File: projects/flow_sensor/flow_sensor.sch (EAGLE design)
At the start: 98 parts, among them IC1 TPS61201, IC5 REG1118

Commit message: Added Spi-Bi-Wire to uC, added SPI connections between uC/NFC
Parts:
- removed J1, J2: (no value), SparkFun-Connectors:CONN_02
- added J3: (no value), SparkFun-Connectors:CONN_07
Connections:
- removed net DATA_CLK: U$2.DATA_CLK
- removed net MISO: U$2.I/O_6
- removed net MOSI: U$2.I/O_7
- removed net N$55: J1.2, U$9.~RESET(SBWTDIO)
- removed net N$56: J1.1, U$9.SBWTCK
- new net 3.3V: J3.3
- new net 5V: J3.2
- new net CLK: U$2.DATA_CLK, U$9.(UCA0CLK/A5)P1.5
- new net RXD: J3.4
- new net SBWTCK: J3.7, U$9.SBWTCK
- new net SBWTDIO: J3.6, U$9.~RESET(SBWTDIO)
- new net SIMO: U$2.I/O_7, U$9.(UCA0TXD/UCA0SIMO)P2.0
- new net SOMI: U$2.I/O_6, U$9.(UCA0RXD/UCA0SOMI)P2.1
- new net STE: U$9.(UCA0STE/A4)P1.4
- new net TXD: J3.5
- net GND: now also J3.1; no longer J2.2
- net VCC: no longer J2.1
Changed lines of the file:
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@@
 <?xml version="1.0" encoding="utf-8"?>
 <!DOCTYPE eagle SYSTEM "eagle.dtd">
-<eagle version="8.5.1">
+<eagle version="8.4.3">
 <drawing>
 <settings>
@@
 <part name="C27" library="SparkFun-Capacitors" deviceset="1.0UF" device="-0603-16V-10%" value="1.0uF"/>
 <part name="C40" library="SparkFun-Capacitors" deviceset="0.1UF" device="-0603-25V-(+80/-20%)" value="0.1uF"/>
-<part name="J1" library="SparkFun-Connectors" deviceset="CONN_02" device=""/>
-<part name="J2" library="SparkFun-Connectors" deviceset="CONN_02" device=""/>
-<part name="GND45" library="SparkFun-PowerSymbols" deviceset="GND2" device=""/>
+<part name="J3" library="SparkFun-Connectors" deviceset="CONN_07" device=""/>
+<part name="GND46" library="SparkFun-PowerSymbols" deviceset="GND2" device=""/>
 </parts>
 <sheets>
@@
 <instance part="C38" gate="G$1" x="96.52" y="2.54"/>
 <instance part="C39" gate="G$1" x="104.14" y="2.54"/>
+<instance part="J3" gate="G$1" x="-63.5" y="20.32" rot="R270"/>
+<instance part="GND46" gate="G$1" x="-68.58" y="2.54"/>
 </instances>
 <busses>
@@
 <wire x1="436.88" y1="-7.62" x2="441.96" y2="-7.62" width="0.1524" layer="91"/>
 <wire x1="441.96" y1="-7.62" x2="441.96" y2="-10.16" width="0.1524" layer="91"/>
+</segment>
+<segment>
+<pinref part="J3" gate="G$1" pin="1"/>
+<wire x1="-68.58" y1="15.24" x2="-68.58" y2="5.08" width="0.1524" layer="91"/>
+<pinref part="GND46" gate="G$1" pin="3.3V"/>
 </segment>
 </net>
@@
 <label x="444.5" y="-35.56" size="1.778" layer="95" rot="MR270"/>
 <pinref part="U$8" gate="G$1" pin="OUT1"/>
+</segment>
+</net>
+<net name="5V" class="0">
+<segment>
+<pinref part="J3" gate="G$1" pin="2"/>
+<wire x1="-66.04" y1="15.24" x2="-66.04" y2="7.62" width="0.1524" layer="91"/>
+<label x="-66.04" y="7.62" size="1.778" layer="95" rot="R270"/>
+</segment>
+</net>
+<net name="3.3V" class="0">
+<segment>
+<pinref part="J3" gate="G$1" pin="3"/>
+<wire x1="-63.5" y1="15.24" x2="-63.5" y2="7.62" width="0.1524" layer="91"/>
+<label x="-63.5" y="7.62" size="1.778" layer="95" rot="R270"/>
+</segment>
+</net>
+<net name="RXD" class="0">
+<segment>
+<pinref part="J3" gate="G$1" pin="4"/>
+<wire x1="-60.96" y1="15.24" x2="-60.96" y2="7.62" width="0.1524" layer="91"/>
+<label x="-60.96" y="7.62" size="1.778" layer="95" rot="R270"/>
+</segment>
+</net>
+<net name="TXD" class="0">
+<segment>
+<pinref part="J3" gate="G$1" pin="5"/>
+<wire x1="-58.42" y1="15.24" x2="-58.42" y2="7.62" width="0.1524" layer="91"/>
+<label x="-58.42" y="7.62" size="1.778" layer="95" rot="R270"/>
+</segment>
+</net>
+<net name="SBWTDIO" class="0">
+<segment>
+<pinref part="J3" gate="G$1" pin="6"/>
+<wire x1="-55.88" y1="15.24" x2="-55.88" y2="7.62" width="0.1524" layer="91"/>
+<label x="-55.88" y="7.62" size="1.778" layer="95" rot="R270"/>
+</segment>
+</net>
+<net name="SBWTCK" class="0">
+<segment>
+<pinref part="J3" gate="G$1" pin="7"/>
+<wire x1="-53.34" y1="15.24" x2="-53.34" y2="7.62" width="0.1524" layer="91"/>
+<label x="-53.34" y="7.62" size="1.778" layer="95" rot="R270"/>
 </segment>
 </net>
@@
 <instance part="C27" gate="G$1" x="218.44" y="43.18" rot="R90"/>
 <instance part="C40" gate="G$1" x="218.44" y="53.34" rot="R90"/>
-<instance part="J1" gate="G$1" x="238.76" y="15.24"/>
-<instance part="J2" gate="G$1" x="233.68" y="17.78" rot="R180"/>
-<instance part="GND45" gate="G$1" x="210.82" y="15.24" rot="R270"/>
 </instances>
 <busses>
@@
 <wire x1="-116.84" y1="45.72" x2="-116.84" y2="53.34" width="0.1524" layer="91"/>
 <label x="-116.84" y="53.34" size="1.6764" layer="95" rot="R90"/>
-</segment>
-</net>
-<net name="DATA_CLK" class="0">
-<segment>
-<pinref part="U$2" gate="G$1" pin="DATA_CLK"/>
-<wire x1="-86.36" y1="43.18" x2="-121.92" y2="43.18" width="0.1524" layer="91"/>
-<wire x1="-121.92" y1="43.18" x2="-121.92" y2="53.34" width="0.1524" layer="91"/>
-<label x="-121.92" y="53.34" size="1.6764" layer="95" rot="R90"/>
-</segment>
-</net>
-<net name="MOSI" class="0">
-<segment>
-<pinref part="U$2" gate="G$1" pin="I/O_7"/>
-<wire x1="-86.36" y1="40.64" x2="-127" y2="40.64" width="0.1524" layer="91"/>
-<wire x1="-127" y1="40.64" x2="-127" y2="53.34" width="0.1524" layer="91"/>
-<label x="-127" y="53.34" size="1.6764" layer="95" rot="R90"/>
-</segment>
-</net>
-<net name="MISO" class="0">
-<segment>
-<pinref part="U$2" gate="G$1" pin="I/O_6"/>
-<wire x1="-86.36" y1="38.1" x2="-132.08" y2="38.1" width="0.1524" layer="91"/>
-<wire x1="-132.08" y1="38.1" x2="-132.08" y2="53.34" width="0.1524" layer="91"/>
-<label x="-132.08" y="53.34" size="1.6764" layer="95" rot="R90"/>
 </segment>
 </net>
@@
 <wire x1="210.82" y1="25.4" x2="256.54" y2="25.4" width="0.1524" layer="91"/>
 </segment>
-<segment>
-<pinref part="J2" gate="G$1" pin="2"/>
-<pinref part="GND45" gate="G$1" pin="3.3V"/>
-<wire x1="226.06" y1="15.24" x2="213.36" y2="15.24" width="0.1524" layer="91"/>
-</segment>
 </net>
 <net name="N$5" class="0">
@@
 <junction x="223.52" y="43.18"/>
 </segment>
-<segment>
-<pinref part="J2" gate="G$1" pin="1"/>
-<wire x1="226.06" y1="17.78" x2="213.36" y2="17.78" width="0.1524" layer="91"/>
-<label x="213.36" y="17.78" size="1.778" layer="95"/>
-</segment>
 </net>
 <net name="N$8" class="0">
@@
 </segment>
 </net>
-<net name="N$55" class="0">
+<net name="SBWTDIO" class="0">
 <segment>
 <pinref part="U$9" gate="G$1" pin="~RESET(SBWTDIO)"/>
-<pinref part="J1" gate="G$1" pin="2"/>
-<wire x1="256.54" y1="17.78" x2="246.38" y2="17.78" width="0.1524" layer="91"/>
-</segment>
-</net>
-<net name="N$56" class="0">
+<wire x1="256.54" y1="17.78" x2="233.68" y2="17.78" width="0.1524" layer="91"/>
+<label x="233.68" y="17.78" size="1.778" layer="95" rot="R180"/>
+</segment>
+</net>
+<net name="SBWTCK" class="0">
 <segment>
 <pinref part="U$9" gate="G$1" pin="SBWTCK"/>
-<pinref part="J1" gate="G$1" pin="1"/>
-<wire x1="256.54" y1="15.24" x2="246.38" y2="15.24" width="0.1524" layer="91"/>
-</segment>
-</net>
+<wire x1="256.54" y1="15.24" x2="233.68" y2="15.24" width="0.1524" layer="91"/>
+<label x="233.68" y="15.24" size="1.778" layer="95" rot="R180"/>
+</segment>
+</net>
+<net name="SIMO" class="0">
+<segment>
+<pinref part="U$9" gate="G$1" pin="(UCA0TXD/UCA0SIMO)P2.0"/>
+<wire x1="317.5" y1="15.24" x2="325.12" y2="15.24" width="0.1524" layer="91"/>
+<label x="325.12" y="15.24" size="1.778" layer="95"/>
+</segment>
+<segment>
+<pinref part="U$2" gate="G$1" pin="I/O_7"/>
+<wire x1="-86.36" y1="40.64" x2="-127" y2="40.64" width="0.1524" layer="91"/>
+<wire x1="-127" y1="40.64" x2="-127" y2="53.34" width="0.1524" layer="91"/>
+<label x="-127" y="53.34" size="1.6764" layer="95" rot="R90"/>
+</segment>
+</net>
+<net name="SOMI" class="0">
+<segment>
+<pinref part="U$9" gate="G$1" pin="(UCA0RXD/UCA0SOMI)P2.1"/>
+<wire x1="317.5" y1="12.7" x2="325.12" y2="12.7" width="0.1524" layer="91"/>
+<label x="325.12" y="12.7" size="1.778" layer="95"/>
+</segment>
+<segment>
+<pinref part="U$2" gate="G$1" pin="I/O_6"/>
+<wire x1="-86.36" y1="38.1" x2="-132.08" y2="38.1" width="0.1524" layer="91"/>
+<wire x1="-132.08" y1="38.1" x2="-132.08" y2="53.34" width="0.1524" layer="91"/>
+<label x="-132.08" y="53.34" size="1.6764" layer="95" rot="R90"/>
+</segment>
+</net>
+<net name="STE" class="0">
+<segment>
+<pinref part="U$9" gate="G$1" pin="(UCA0STE/A4)P1.4"/>
+<wire x1="317.5" y1="30.48" x2="325.12" y2="30.48" width="0.1524" layer="91"/>
+<label x="325.12" y="30.48" size="1.778" layer="95"/>
+</segment>
+</net>
+<net name="CLK" class="0">
+<segment>
+<pinref part="U$9" gate="G$1" pin="(UCA0CLK/A5)P1.5"/>
+<wire x1="317.5" y1="27.94" x2="325.12" y2="27.94" width="0.1524" layer="91"/>
+<label x="325.12" y="27.94" size="1.778" layer="95"/>
+</segment>
+<segment>
+<pinref part="U$2" gate="G$1" pin="DATA_CLK"/>
+<wire x1="-86.36" y1="43.18" x2="-121.92" y2="43.18" width="0.1524" layer="91"/>
+<wire x1="-121.92" y1="43.18" x2="-121.92" y2="53.34" width="0.1524" layer="91"/>
+<label x="-121.92" y="53.34" size="1.6764" layer="95" rot="R90"/>
+</segment>
+</net>

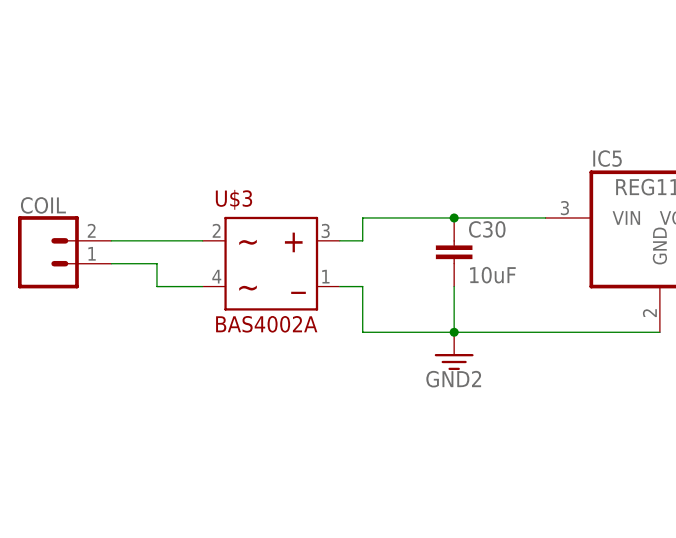
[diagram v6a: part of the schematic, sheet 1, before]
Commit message: Fixed BAS4002A part again
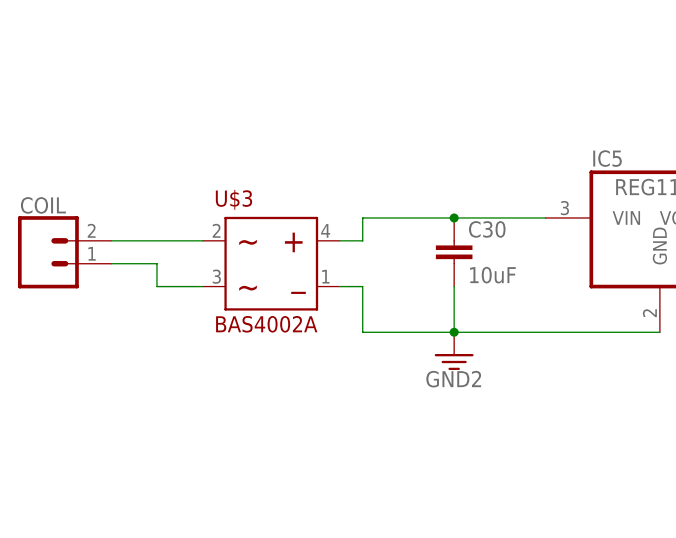
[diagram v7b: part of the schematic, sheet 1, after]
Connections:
- net N$1 renamed POWERCOIL
- net N$27 renamed POWERCOIL'
- net N$30 renamed UNREG+
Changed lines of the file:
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@@
 <?xml version="1.0" encoding="utf-8"?>
 <!DOCTYPE eagle SYSTEM "eagle.dtd">
-<eagle version="8.4.3">
+<eagle version="8.5.1">
 <drawing>
 <settings>
@@
 </segment>
 </net>
-<net name="N$1" class="0">
+<net name="POWERCOIL" class="0">
 <segment>
 <pinref part="COIL" gate="G$1" pin="2"/>
@@
 </segment>
 </net>
-<net name="N$30" class="0">
+<net name="UNREG+" class="0">
 <segment>
 <pinref part="U$3" gate="G$1" pin="+"/>
@@
 </segment>
 </net>
-<net name="N$27" class="0">
+<net name="POWERCOIL'" class="0">
 <segment>
 <pinref part="U$3" gate="G$1" pin="~'"/>

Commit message: Modified sensor: Added mux, reduced op-amps
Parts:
- removed C29, C31, C32, C33, C34, C35, C36: 3uF, SparkFun-Capacitors:4.7UF0603
- removed R16, R17, R18, R19, R20, R21: 10k, SparkFun-Resistors:10KOHM-0603-1/10W-1%
- removed R37: 1.5k, SparkFun-Resistors:8.2KOHM-0603-1/10W-5%
- removed R38: 1.5k, SparkFun-Resistors:1.5KOHM-0603-1/10W-1%
- removed R39: 8.2k, SparkFun-Resistors:1.5KOHM-0603-1/10W-1%
- removed U$5: LM2902, my_library:LM2902
- added C41: 3uF, SparkFun-Capacitors:4.7UF0603
- R11, R29: value 600 -> 8.2k; device SparkFun-Resistors:680OHM-0603-1/10W-5% -> SparkFun-Resistors:8.2KOHM-0603-1/10W-5%
- R22: value 800 -> 1.5k; device SparkFun-Resistors:787OHM-0603-1/10W-1% -> SparkFun-Resistors:8.2KOHM-0603-1/10W-5%
- R23: value 600 -> 1.5k; device SparkFun-Resistors:680OHM-0603-1/10W-5% -> SparkFun-Resistors:1.5KOHM-0603-1/10W-1%
- R24, R31: device SparkFun-Resistors:8.2KOHM-0603-1/10W-5% -> SparkFun-Resistors:1.5KOHM-0603-1/10W-1%
- R25, R32: value 1.5k -> 8.2k
- R26: device SparkFun-Resistors:1.5KOHM-0603-1/10W-1% -> SparkFun-Resistors:8.2KOHM-0603-1/10W-5%
- R27, R30: value 8.2k -> 1.5k
- R28: value 800 -> 8.2k; device SparkFun-Resistors:787OHM-0603-1/10W-1% -> SparkFun-Resistors:1.5KOHM-0603-1/10W-1%
- R33: value 8.2k -> 800; device SparkFun-Resistors:1.5KOHM-0603-1/10W-1% -> SparkFun-Resistors:787OHM-0603-1/10W-1%
- R35: value 600 -> 800; device SparkFun-Resistors:680OHM-0603-1/10W-5% -> SparkFun-Resistors:787OHM-0603-1/10W-1%
- R36: value 8.2k -> 600; device SparkFun-Resistors:8.2KOHM-0603-1/10W-5% -> SparkFun-Resistors:787OHM-0603-1/10W-1%
- U$7: value AD8222 -> MAX4634; device my_library:AD8222 -> my_library:MAX4634
- U$8: value AD8222 -> AD8295; device my_library:AD8222 -> my_library:AD8295
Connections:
- removed net N$31: C34.1, R16.2, R17.1
- removed net N$36: C31.1, R17.2
- removed net N$38: C35.1, R18.2, R19.1
- removed net N$39: C32.1, R19.2
- removed net N$41: C36.1, R20.2, R21.1
- removed net N$42: C33.1, R21.2
- removed net N$47: R22.1, U$6.RG2
- removed net N$49: R23.1, U$6.RG1
- removed net N$52: R34.2, U$8.RG2'
- removed net N$53: R35.1, U$8.RG1
- removed net N$54: R35.2, U$8.RG1'
- removed net OPAMP1_OUT: C29.2, U$4.+IN1, U$5.IN1-, U$5.OUT1
- removed net OPAMP2_OUT: C34.2, U$5.IN2-, U$5.OUT2, U$6.+IN1
- removed net OPAMP3_IN: R18.1, U$7.OUT2
- removed net OPAMP3_OUT: C35.2, U$5.IN3-, U$5.OUT3, U$7.+IN1
- removed net OPAMP4_IN: R20.1, U$8.OUT2
- removed net OPAMP4_OUT: C36.2, U$5.IN4-, U$5.OUT4, U$8.+IN1
- removed net SENSOR_ADC1: U$4.OUT1
- removed net SENSOR_ADC2: U$6.OUT1
- removed net SENSOR_ADC3: U$7.OUT1
- removed net SENSOR_ADC4: U$8.OUT1
- new net MUX_A0: U$7.A0
- new net MUX_A1: U$7.A1
- new net MUX_EN: U$7.EN
- new net N$1: R11.2, R23.1, U$4.-IN2
- new net N$27: R30.1, R32.2, U$6.+IN2
- new net N$30: R33.1, U$6.RG2
- new net SENSOR_OUT: U$8.OUT
- net 3.3V: now also U$7.GND, U$8.-IN
- net GND: now also R22.2, R23.2, R27.2, R30.2; no longer C31.2, C32.2, C33.2, R25.2, R32.2, R37.2, R38.2, U$4.-IN1, U$5.VCC-, U$6.-IN1, U$7.-IN1, U$7.-VS, U$7.REF1, U$7.REF2, U$8.-IN1, U$8.-VS, U$8.REF1, U$8.REF2
- net N$18: now also U$7.COM; no longer U$4.OUT2
- net N$19: now also U$8.A2+IN; no longer U$5.IN1+
- net N$21: now also R22.1, R24.2, U$4.+IN2; no longer R16.1, U$6.OUT2
- net N$22: now also R25.2, R27.1, U$6.-IN1; no longer R36.2, R38.1, U$8.-IN2
- net N$25: now also R26.1, R28.2, U$6.+IN1; no longer R11.1, U$4.RG1
- net N$26: now also R29.2, R31.1, U$6.-IN2; no longer R11.2, U$4.RG1'
- net N$28: now also U$4.-IN1; no longer U$4.-IN2
- net N$29: now also U$4.+IN1; no longer U$4.+IN2
- net N$32: now also R33.2, U$6.RG2'; no longer R30.2, R32.1, U$7.-IN2
- net N$33: now also R34.1, U$6.RG1; no longer R31.1, R33.2, U$7.+IN2
- net N$34: now also R34.2, U$6.RG1'; no longer R28.1, U$7.RG2
- net N$35: now also C41.1; no longer C29.1
- net N$37: now also R35.1; no longer R37.1, R39.2, U$8.+IN2
- net N$40: now also R35.2; no longer R34.1, U$8.RG2
- net N$43: now also U$4.OUT1, U$7.NO1; no longer R24.2, R26.1, U$6.-IN2
- net N$44: now also U$4.OUT2, U$7.NO2; no longer R25.1, R27.2, U$6.+IN2
- net N$45: now also U$6.OUT1, U$7.NO3; no longer R28.2, U$7.RG2'
- net N$46: now also U$6.OUT2, U$7.NO4; no longer R29.1, U$7.RG1
- net N$48: now also C41.2, U$8.+IN, U$8.A2-IN, U$8.A2OUT; no longer R22.2, U$6.RG2'
- net N$50: now also R36.2, U$8.RG'; no longer R23.2, U$6.RG1'
- net N$51: now also R36.1, U$8.RG; no longer R29.2, U$7.RG1'
- net VCC: now also R11.1, R25.1, R28.1, R29.1, R32.1, U$7.V+; no longer R27.1, R30.1, R33.1, R36.1, R39.1, U$5.VCC+, U$7.+VS, U$8.+VS
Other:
- moved on the sheet: C28, R10, R11, R12, R13, R14, R15, R22, R23, R24, R25, R26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
